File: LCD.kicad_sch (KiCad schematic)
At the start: 4 parts

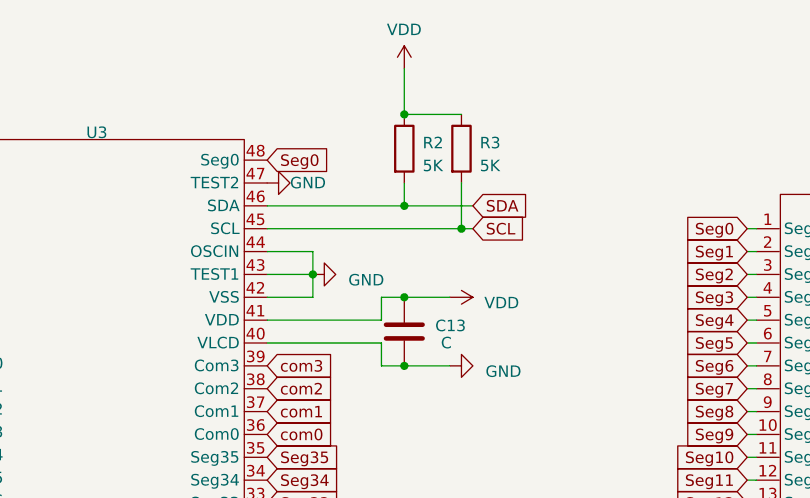
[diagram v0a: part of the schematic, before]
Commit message: Adjusted the VDD supply schematic
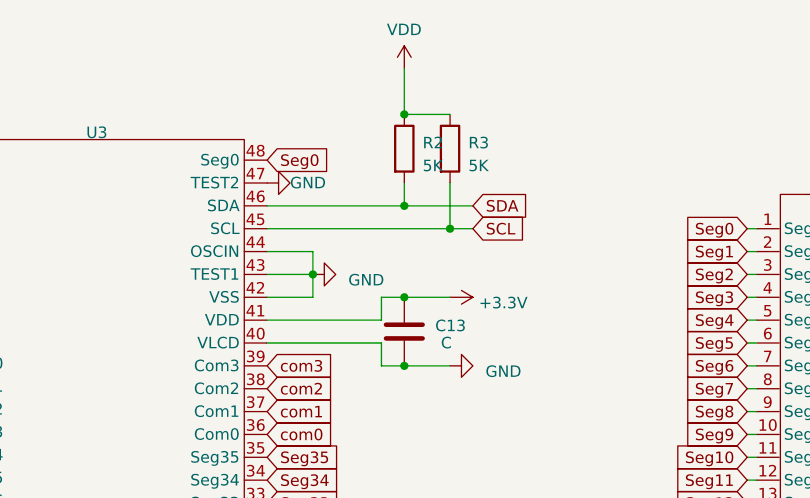
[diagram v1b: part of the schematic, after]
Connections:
- net VDD: no longer C13.1, U3.41 (VDD)
- new net +3.3V: C13.1, U3.41 (VDD)
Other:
- moved on the sheet: R3
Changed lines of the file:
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@@
     (rev "1.0")
   )
-  (junction (at 125.73 71.12) (diameter 0) (color 0 0 0 0)
-  )
   (junction (at 119.38 78.74) (diameter 0) (color 0 0 0 0)
   )
@@
   (junction (at 119.38 86.36) (diameter 0) (color 0 0 0 0)
   )
+  (junction (at 124.46 71.12) (diameter 0) (color 0 0 0 0)
+  )
   (junction (at 119.38 68.58) (diameter 0) (color 0 0 0 0)
   )
@@
     (stroke (width 0) (type default))
   )
-  (wire (pts (xy 125.73 66.04) (xy 125.73 71.12))
+  (wire (pts (xy 124.46 66.04) (xy 124.46 71.12))
     (stroke (width 0) (type default))
   )
@@
     (stroke (width 0) (type default))
   )
-  (wire (pts (xy 104.14 71.12) (xy 125.73 71.12))
-    (stroke (width 0) (type default))
-  )
   (wire (pts (xy 65.786 116.586) (xy 66.294 116.586))
     (stroke (width 0) (type default))
@@
     (stroke (width 0) (type default))
   )
-  (wire (pts (xy 125.73 71.12) (xy 127 71.12))
-    (stroke (width 0) (type default))
-  )
   (wire (pts (xy 157.48 101.6) (xy 158.496 101.6))
     (stroke (width 0) (type default))
@@
     (stroke (width 0) (type default))
   )
+  (wire (pts (xy 104.14 71.12) (xy 124.46 71.12))
+    (stroke (width 0) (type default))
+  )
   (wire (pts (xy 65.786 88.646) (xy 66.294 88.646))
     (stroke (width 0) (type default))
   )
-  (wire (pts (xy 119.38 58.42) (xy 125.73 58.42))
+  (wire (pts (xy 119.38 58.42) (xy 124.46 58.42))
     (stroke (width 0) (type default))
   )
@@
   )
   (wire (pts (xy 104.14 73.66) (xy 109.22 73.66))
+    (stroke (width 0) (type default))
+  )
+  (wire (pts (xy 124.46 71.12) (xy 127 71.12))
     (stroke (width 0) (type default))
   )
@@
         (path "/82b2e9f2-0f9f-45f5-b878-35b85461c206/dda7952a-6652-4e1c-bc88-abda2479a8df"
           (reference "#PWR07") (unit 1)
-        )
-      )
-    )
-  )
-  (symbol (lib_id "power:VDD") (at 124.46 78.74 270) (unit 1)
-    (in_bom yes) (on_board yes) (dnp no) (fields_autoplaced)
-    (property "Reference" "#PWR08" (at 120.65 78.74 0)
-      (effects (font (size 1.27 1.27)) hide)
-    )
-    (property "Value" "VDD" (at 128.27 79.375 90)
-      (effects (font (size 1.27 1.27)) (justify left))
-    )
-    (property "Footprint" "" (at 124.46 78.74 0)
-      (effects (font (size 1.27 1.27)) hide)
-    )
-    (property "Datasheet" "" (at 124.46 78.74 0)
-      (effects (font (size 1.27 1.27)) hide)
-    )
-    (pin "1")
-    (instances
-      (project "power_supply"
-        (path "/82b2e9f2-0f9f-45f5-b878-35b85461c206/dda7952a-6652-4e1c-bc88-abda2479a8df"
-          (reference "#PWR08") (unit 1)
         )
       )
@@
     )
   )
-  (symbol (lib_id "Device:R") (at 125.73 62.23 0) (unit 1)
+  (symbol (lib_id "Device:R") (at 124.46 62.23 0) (unit 1)
     (in_bom yes) (on_board yes) (dnp no) (fields_autoplaced)
-    (property "Reference" "R3" (at 127.762 61.595 0)
+    (property "Reference" "R3" (at 126.492 61.595 0)
       (effects (font (size 1.27 1.27)) (justify left))
     )
-    (property "Value" "5K" (at 127.762 64.135 0)
+    (property "Value" "5K" (at 126.492 64.135 0)
       (effects (font (size 1.27 1.27)) (justify left))
     )
-    (property "Footprint" "" (at 123.952 62.23 90)
-      (effects (font (size 1.27 1.27)) hide)
-    )
-    (property "Datasheet" "~" (at 125.73 62.23 0)
+    (property "Footprint" "" (at 122.682 62.23 90)
+      (effects (font (size 1.27 1.27)) hide)
+    )
+    (property "Datasheet" "~" (at 124.46 62.23 0)
       (effects (font (size 1.27 1.27)) hide)
     )
@@
         )
       )
+    )
+  )
+  (symbol (lib_id "power:+3.3V") (at 124.46 78.74 270) (unit 1)
+    (in_bom yes) (on_board yes) (dnp no) (fields_autoplaced)
+    (property "Reference" "#PWR08" (at 120.65 78.74 0)
+      (effects (font (size 1.27 1.27)) hide)
+    )
+    (property "Value" "+3.3V" (at 127.6604 79.375 90)
+      (effects (font (size 1.27 1.27)) (justify left))
+    )
+    (property "Footprint" "" (at 124.46 78.74 0)
+      (effects (font (size 1.27 1.27)) hide)
+    )
+    (property "Datasheet" "" (at 124.46 78.74 0)
+      (effects (font (size 1.27 1.27)) hide)
+    )
+    (pin "1")
+    (instances
+      (project "power_supply"
+        (path "/82b2e9f2-0f9f-45f5-b878-35b85461c206/dda7952a-6652-4e1c-bc88-abda2479a8df"
+          (reference "#PWR08") (unit 1)
+        )
+      )
